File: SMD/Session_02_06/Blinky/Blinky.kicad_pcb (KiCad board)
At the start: 2 copper layers, 30 x 30 mm, 15 parts, among them U1 TLC551CD‎

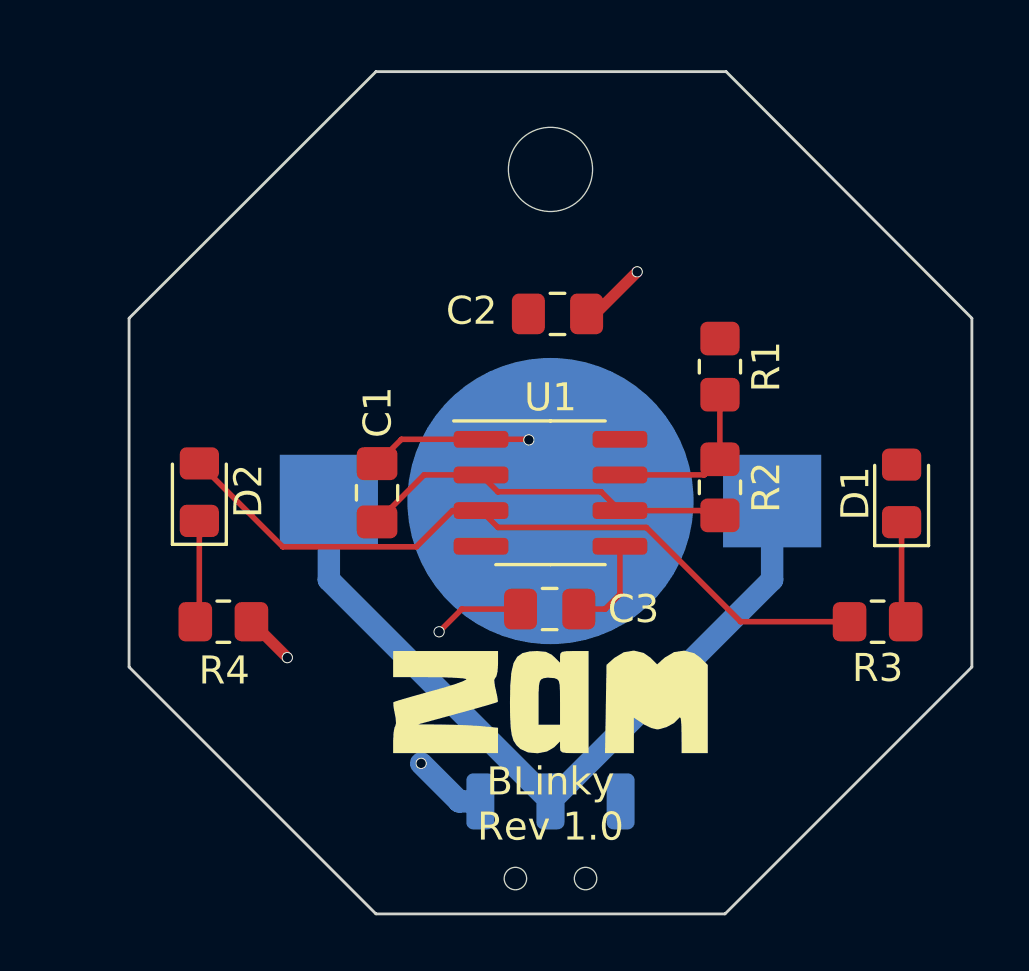
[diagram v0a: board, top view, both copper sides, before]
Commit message: Makes corrections to the design rules
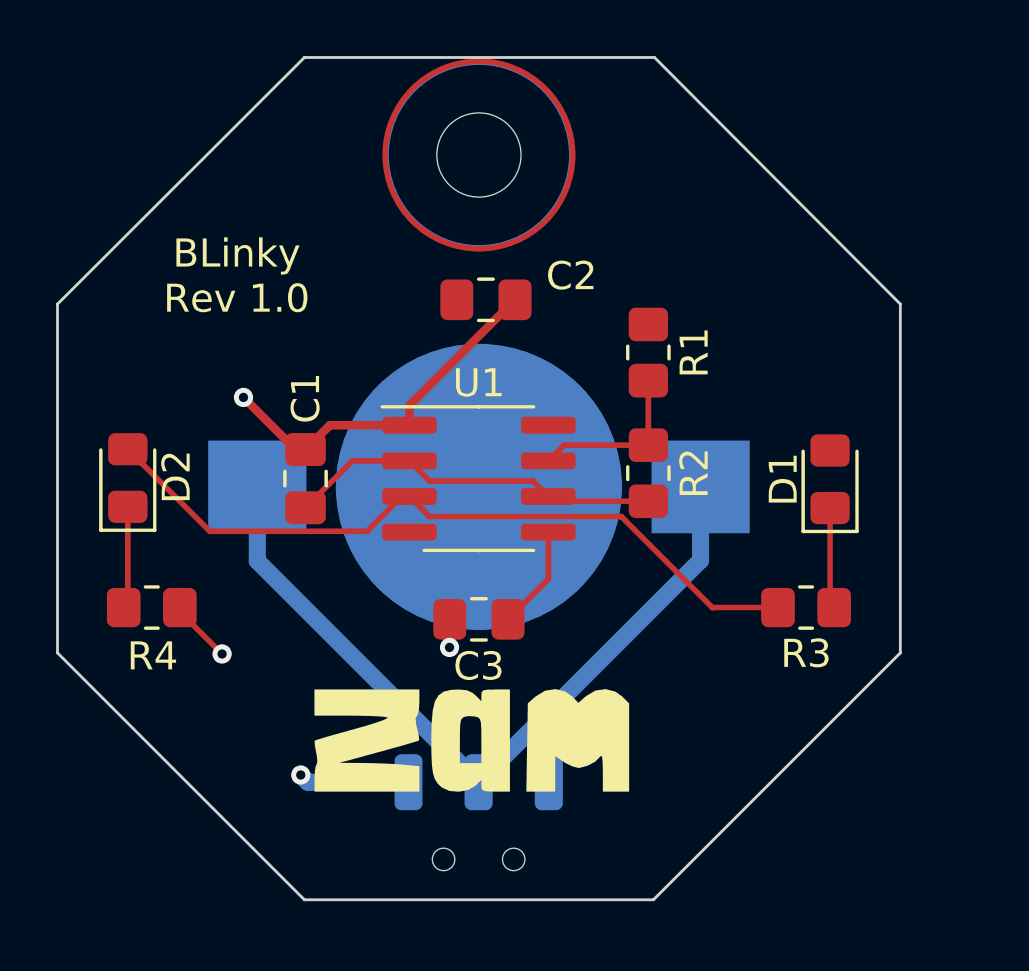
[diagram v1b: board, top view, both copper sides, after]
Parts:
- removed LG?: LOGO, Blinky_ZAM:ZAM_LOGO_440
- moved LG2 3.12 mm to (190.2, 62.5)
- moved SW? 2.65 mm to (190.5, 64.0)
- moved H? 2.60 mm to (190.5, 41.7)
- moved BT1 2.60 mm to (190.5, 53.5)
- moved C1 2.60 mm to (184.3, 53.2)
- moved C2 2.60 mm to (190.7, 46.8)
- moved D1 2.60 mm to (203.0, 53.2)
- moved D2 2.60 mm to (178.0, 53.2)
- moved R1 2.60 mm to (196.5, 48.7)
- moved R2 2.60 mm to (196.5, 53.0)
- moved R3 2.60 mm to (202.2, 57.8)
- moved U1 2.60 mm to (190.5, 53.2)
- moved R4 2.60 mm to (178.8, 57.8)
- moved C3 2.55 mm to (190.5, 58.2)
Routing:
- net GND: track 13.2 -> 16.4 mm, vias 4 -> 3
- net /VCC: track 2.67 -> 3.95 mm

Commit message: Corrections to the switch footprint
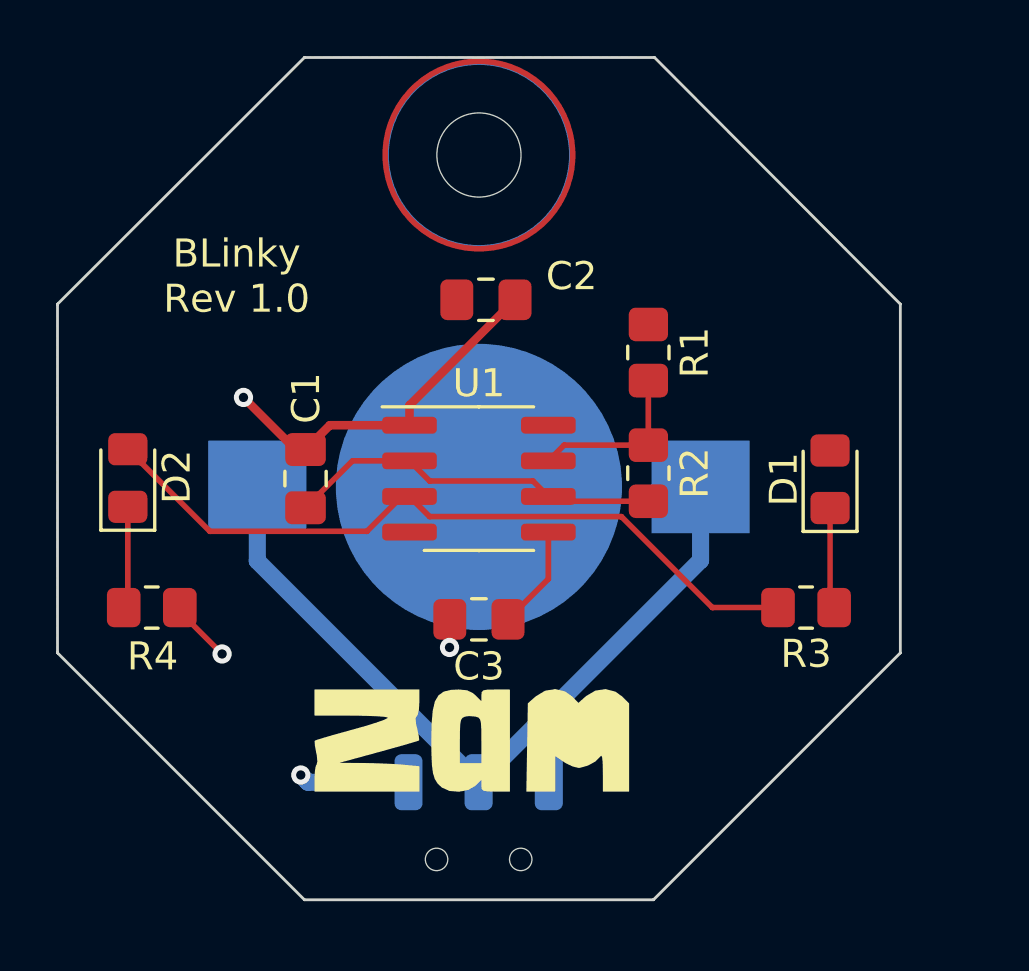
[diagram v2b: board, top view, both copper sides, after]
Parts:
- turned BT1 to 0 degrees
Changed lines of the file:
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@@
       (effects (font (size 1 1) (thickness 0.15)) (justify mirror))
     )
+    (fp_rect (start -3.500001 1.1) (end 3.500001 4) (layer "B.SilkS") (width 0.1524) (fill none))
     (fp_rect (start -2 5.499999) (end -0.5 4) (layer "B.SilkS") (width 0.1524) (fill none))
-    (fp_rect (start -3.500001 1.1) (end 3.5 4) (layer "B.SilkS") (width 0.1524) (fill none))
     (fp_rect (start -3.5 5.5) (end 3.5 -1) (layer "B.CrtYd") (width 0.01) (fill none))
-    (pad "" np_thru_hole circle (at -1.25 2.75) (size 0.8 0.8) (drill 0.8) (layers F&B.Cu *.Mask))
-    (pad "" np_thru_hole circle (at 1.25 2.75) (size 0.8 0.8) (drill 0.8) (layers F&B.Cu *.Mask))
+    (pad "" np_thru_hole circle (at -1.5 2.75) (size 0.8 0.8) (drill 0.8) (layers F&B.Cu *.Mask))
+    (pad "" np_thru_hole circle (at 1.5 2.75) (size 0.8 0.8) (drill 0.8) (layers F&B.Cu *.Mask))
     (pad "1" smd roundrect (at -2.5 0) (size 1 2) (layers "B.Cu" "B.Paste" "B.Mask") (roundrect_rratio 0.25)
       (net 4 "/VCC") (pinfunction "A") (pintype "passive"))
@@
   )
   (footprint "Battery:BatteryHolder_Keystone_3000_1x12mm" (layer "B.Cu")
-    (at 190.499683 53.486392 180)
+    (at 190.499683 53.486392)
     (descr "http://www.keyelco.com/product-pdf.cfm?p=777")
     (tags "Keystone type 3000 coin cell retainer")
@@
     (fp_arc (start -5.378013 -5.447558) (mid -4.942443 -5.378013) (end -4.6 -5.1) (layer "B.Fab") (width 0.1))
     (fp_arc (start 5.3 -5.45) (mid 6.239949 -5.019238) (end 6.6 -4.05) (layer "B.Fab") (width 0.1))
-    (pad "1" smd rect (at 7.9 0 180) (size 3.5 3.3) (layers "B.Cu" "B.Paste" "B.Mask")
+    (pad "1" smd rect (at 7.9 0) (size 3.5 3.3) (layers "B.Cu" "B.Paste" "B.Mask")
       (net 1 "Net-(BT1-Pad1)") (pinfunction "+") (pintype "passive"))
-    (pad "1" smd rect (at -7.9 0 180) (size 3.5 3.3) (layers "B.Cu" "B.Paste" "B.Mask")
+    (pad "1" smd rect (at -7.9 0) (size 3.5 3.3) (layers "B.Cu" "B.Paste" "B.Mask")
       (net 1 "Net-(BT1-Pad1)") (pinfunction "+") (pintype "passive"))
-    (pad "2" smd circle (at 0 0 180) (size 10.2 10.2) (layers "B.Cu" "B.Mask")
+    (pad "2" smd circle (at 0 0) (size 10.2 10.2) (layers "B.Cu" "B.Mask")
       (net 2 "GND") (pinfunction "-") (pintype "passive"))
     (model "${KICAD6_3DMODEL_DIR}/Battery.3dshapes/BatteryHolder_Keystone_3000_1x12mm.wrl"
